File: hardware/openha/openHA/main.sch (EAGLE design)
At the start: 69 parts, among them IC1 MBN52832, J1 HP_Con, J2 MICRO-USB-RECEPTACLE47589-0001, J3 Bat_Con, U1 STM32L476JX, U2 PCM1774RGPR, U4 STG3693QTR, U5 STBCFG01JR, U6 LD39115J, U7 LD39115J, X1 32.768kHz

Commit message: WIP-BOM Update
Update USB case
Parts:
- added L1: 330Ohms - 600mA, OAlib:L_EMI0402
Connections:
- removed net GND: C26.2, C27.2, C41.2, IC1.GND_1, IC1.GND_2, IC1.GND_3, IC1.GND_4, IC1.GND_5, IC1.GND_6, IC1.GND_7, IC1.GND_8
- new net N$12: D3.A, J2.1, L3.2
- new net N$8: J2.CASE, L1.1
- net DGND: now also C26.2, C27.2, C41.2, IC1.GND_1, IC1.GND_2, IC1.GND_3, IC1.GND_4, IC1.GND_5, IC1.GND_6, IC1.GND_7, IC1.GND_8, L1.2; no longer J2.GND1, J2.GND2, J2.GND3, J2.GND4
- net V_USB: no longer D3.A, J2.1, L3.2
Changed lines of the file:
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@@
 <part name="C20" library="OAlib" deviceset="C_NP" device="0603" package3d_urn="urn:adsk.eagle:package:3714360/1" value="4.7uF"/>
 <part name="R12" library="OAlib" deviceset="R" device="" package3d_urn="urn:adsk.eagle:package:3714360/1" value="10k"/>
+<part name="L1" library="OAlib" deviceset="L_EMI" device="0402" package3d_urn="urn:adsk.eagle:package:23626/2" value="330Ohms - 600mA"/>
 </parts>
 <sheets>
@@
 </segment>
 </net>
-<net name="GND" class="0">
+<net name="DGND" class="0">
 <segment>
 <pinref part="C26" gate="A" pin="2"/>
@@
 <attribute name="VALUE" x="16.764" y="188.341" size="1.778" layer="96" font="vector"/>
 </instance>
-<instance part="SUPPLY17" gate="DGND" x="38.1" y="144.78" smashed="yes">
-<attribute name="VALUE" x="36.195" y="141.605" size="1.778" layer="96"/>
+<instance part="SUPPLY17" gate="DGND" x="38.1" y="119.38" smashed="yes">
+<attribute name="VALUE" x="36.195" y="116.205" size="1.778" layer="96"/>
 </instance>
 <instance part="SUPPLY20" gate="AGND" x="-60.96" y="86.36" smashed="yes">
@@
 </instance>
 <instance part="U4" gate="G$1" x="-10.16" y="154.94" smashed="yes" rot="R90">
-<attribute name="NAME" x="3.81" y="139.7" size="1.778" layer="95" rot="R180" align="center-left"/>
+<attribute name="NAME" x="1.27" y="139.7" size="1.778" layer="95" align="center-left"/>
 <attribute name="VALUE" x="1.27" y="137.16" size="1.778" layer="96" align="center-left"/>
 </instance>
@@
 <attribute name="NAME" x="-26.416" y="100.711" size="1.778" layer="95" font="vector"/>
 <attribute name="VALUE" x="-21.082" y="100.711" size="1.778" layer="96" font="vector"/>
+</instance>
+<instance part="L1" gate="G$1" x="43.18" y="139.7" smashed="yes" rot="R270">
+<attribute name="NAME" x="49.022" y="141.986" size="1.778" layer="95" rot="R270" align="center-left"/>
+<attribute name="VALUE" x="46.482" y="141.986" size="1.778" layer="96" rot="R270" align="center-left"/>
 </instance>
 </instances>
@@
 </net>
 <net name="V_USB" class="0">
-<segment>
-<pinref part="D3" gate="G$1" pin="A"/>
-<pinref part="L3" gate="G$1" pin="2"/>
-<wire x1="27.94" y1="198.12" x2="38.1" y2="198.12" width="0.1524" layer="91"/>
-<wire x1="38.1" y1="198.12" x2="38.1" y2="170.18" width="0.1524" layer="91"/>
-<junction x="27.94" y="198.12"/>
-<pinref part="J2" gate="G$1" pin="1"/>
-<wire x1="38.1" y1="170.18" x2="40.64" y2="170.18" width="0.1524" layer="91"/>
-<wire x1="27.94" y1="198.12" x2="27.94" y2="190.5" width="0.1524" layer="91"/>
-</segment>
 <segment>
 <pinref part="L3" gate="G$1" pin="1"/>
@@
 <pinref part="U4" gate="G$1" pin="VCC"/>
 <wire x1="-10.16" y1="137.16" x2="-10.16" y2="124.46" width="0.1524" layer="91"/>
-<label x="-10.16" y="137.16" size="1.778" layer="95" rot="R270"/>
+<label x="-11.938" y="137.16" size="1.778" layer="95" rot="R270"/>
 </segment>
 </net>
@@
 <segment>
 <wire x1="-5.08" y1="137.16" x2="-5.08" y2="124.46" width="0.1524" layer="91"/>
-<label x="-5.08" y="137.16" size="1.778" layer="95" rot="R270"/>
+<label x="-6.858" y="137.16" size="1.778" layer="95" rot="R270"/>
 <pinref part="U4" gate="G$1" pin="2S1"/>
 </segment>
@@
 <pinref part="U4" gate="G$1" pin="1S2"/>
 <wire x1="-12.7" y1="137.16" x2="-12.7" y2="124.46" width="0.1524" layer="91"/>
-<label x="-12.7" y="137.16" size="1.778" layer="95" rot="R270"/>
+<label x="-14.478" y="137.16" size="1.778" layer="95" rot="R270"/>
 </segment>
 </net>
@@
 </segment>
 <segment>
+<pinref part="J2" gate="G$1" pin="5"/>
+<wire x1="38.1" y1="160.02" x2="40.64" y2="160.02" width="0.1524" layer="91"/>
 <pinref part="SUPPLY17" gate="DGND" pin="GND"/>
-<wire x1="38.1" y1="147.32" x2="38.1" y2="149.86" width="0.1524" layer="91"/>
-<wire x1="38.1" y1="149.86" x2="38.1" y2="160.02" width="0.1524" layer="91"/>
-<wire x1="38.1" y1="160.02" x2="40.64" y2="160.02" width="0.1524" layer="91"/>
-<pinref part="J2" gate="G$1" pin="5"/>
-<pinref part="J2" gate="G$1" pin="GND1"/>
-<wire x1="43.18" y1="152.4" x2="43.18" y2="149.86" width="0.1524" layer="91"/>
-<wire x1="43.18" y1="149.86" x2="38.1" y2="149.86" width="0.1524" layer="91"/>
-<junction x="38.1" y="149.86"/>
-<pinref part="J2" gate="G$1" pin="GND2"/>
-<wire x1="45.72" y1="152.4" x2="45.72" y2="149.86" width="0.1524" layer="91"/>
-<wire x1="45.72" y1="149.86" x2="43.18" y2="149.86" width="0.1524" layer="91"/>
-<junction x="43.18" y="149.86"/>
-<pinref part="J2" gate="G$1" pin="GND3"/>
-<wire x1="48.26" y1="152.4" x2="48.26" y2="149.86" width="0.1524" layer="91"/>
-<wire x1="48.26" y1="149.86" x2="45.72" y2="149.86" width="0.1524" layer="91"/>
-<junction x="45.72" y="149.86"/>
-<pinref part="J2" gate="G$1" pin="GND4"/>
-<wire x1="50.8" y1="152.4" x2="50.8" y2="149.86" width="0.1524" layer="91"/>
-<wire x1="50.8" y1="149.86" x2="48.26" y2="149.86" width="0.1524" layer="91"/>
-<junction x="48.26" y="149.86"/>
+<wire x1="38.1" y1="121.92" x2="38.1" y2="129.54" width="0.1524" layer="91"/>
+<pinref part="L1" gate="G$1" pin="2"/>
+<wire x1="38.1" y1="129.54" x2="38.1" y2="160.02" width="0.1524" layer="91"/>
+<wire x1="43.18" y1="134.62" x2="43.18" y2="129.54" width="0.1524" layer="91"/>
+<wire x1="43.18" y1="129.54" x2="38.1" y2="129.54" width="0.1524" layer="91"/>
+<junction x="38.1" y="129.54"/>
 </segment>
 </net>
@@
 <pinref part="U4" gate="G$1" pin="1-2-3SEL"/>
 <wire x1="-7.62" y1="137.16" x2="-7.62" y2="124.46" width="0.1524" layer="91"/>
-<label x="-7.62" y="137.16" size="1.778" layer="95" rot="R270"/>
-</segment>
-</net>
+<label x="-9.398" y="137.16" size="1.778" layer="95" rot="R270"/>
+</segment>
+</net>
+<net name="N$8" class="0">
+<segment>
+<pinref part="J2" gate="G$1" pin="CASE"/>
+<wire x1="48.26" y1="152.4" x2="48.26" y2="149.86" width="0.1524" layer="91"/>
+<pinref part="L1" gate="G$1" pin="1"/>
+<wire x1="48.26" y1="149.86" x2="43.18" y2="149.86" width="0.1524" layer="91"/>
+<wire x1="43.18" y1="149.86" x2="43.18" y2="144.78" width="0.1524" layer="91"/>
+</segment>
+</net>
+<net name="N$12" class="0">
+<segment>
+<pinref part="L3" gate="G$1" pin="2"/>
+<pinref part="D3" gate="G$1" pin="A"/>
+<wire x1="27.94" y1="198.12" x2="27.94" y2="190.5" width="0.1524" layer="91"/>
+<wire x1="27.94" y1="198.12" x2="38.1" y2="198.12" width="0.1524" layer="91"/>
+<wire x1="38.1" y1="198.12" x2="38.1" y2="170.18" width="0.1524" layer="91"/>
+<junction x="27.94" y="198.12"/>
+<pinref part="J2" gate="G$1" pin="1"/>
+<wire x1="38.1" y1="170.18" x2="40.64" y2="170.18" width="0.1524" layer="91"/>
+</segment>
+</net>

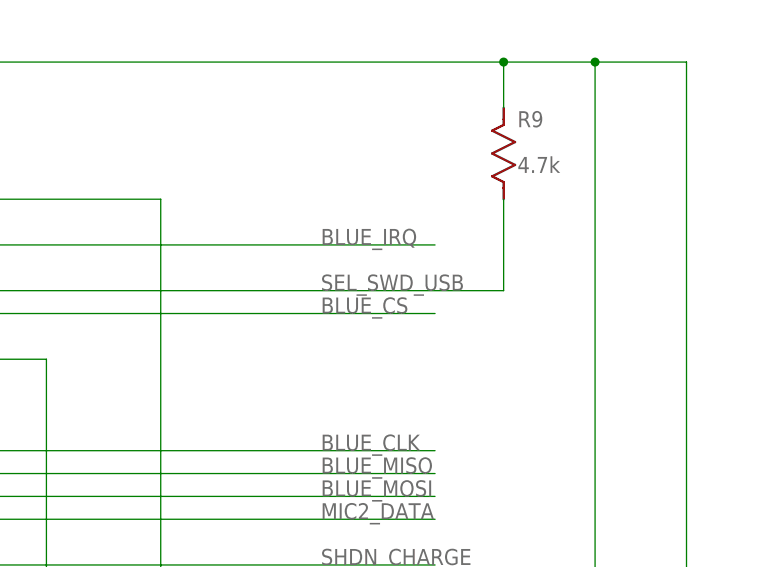
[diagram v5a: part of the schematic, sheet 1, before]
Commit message: Footprint update
Update some footprint
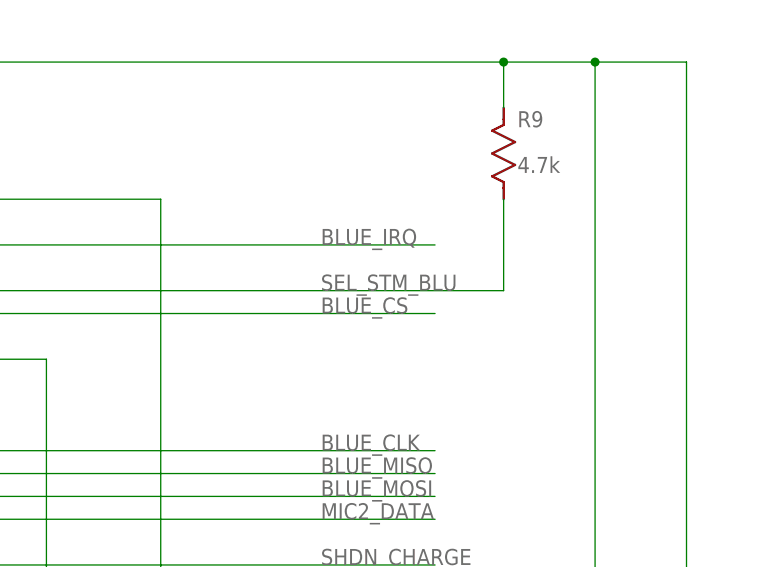
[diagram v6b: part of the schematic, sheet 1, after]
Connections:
- net SEL_STM_BLU: now also R9.2, U1.PB1
- net SEL_SWD_USB: no longer R9.2, U1.PB1
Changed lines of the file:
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@@
 <wire x1="-55.88" y1="-50.8" x2="-55.88" y2="-48.26" width="0.1524" layer="91"/>
-</segment>
-<segment>
-<pinref part="U1" gate="A" pin="PB1"/>
-<wire x1="78.74" y1="20.32" x2="177.8" y2="20.32" width="0.1524" layer="91"/>
-<label x="157.48" y="20.32" size="1.778" layer="95"/>
-<pinref part="R9" gate="R1" pin="2"/>
-<wire x1="177.8" y1="30.48" x2="177.8" y2="20.32" width="0.1524" layer="91"/>
 </segment>
 </net>
@@
 </segment>
 </net>
+<net name="SEL_STM_BLU" class="0">
+<segment>
+<pinref part="U1" gate="A" pin="PB1"/>
+<wire x1="78.74" y1="20.32" x2="177.8" y2="20.32" width="0.1524" layer="91"/>
+<label x="157.48" y="20.32" size="1.778" layer="95"/>
+<pinref part="R9" gate="R1" pin="2"/>
+<wire x1="177.8" y1="30.48" x2="177.8" y2="20.32" width="0.1524" layer="91"/>
+</segment>
+</net>
